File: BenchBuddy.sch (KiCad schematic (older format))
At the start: 0 parts

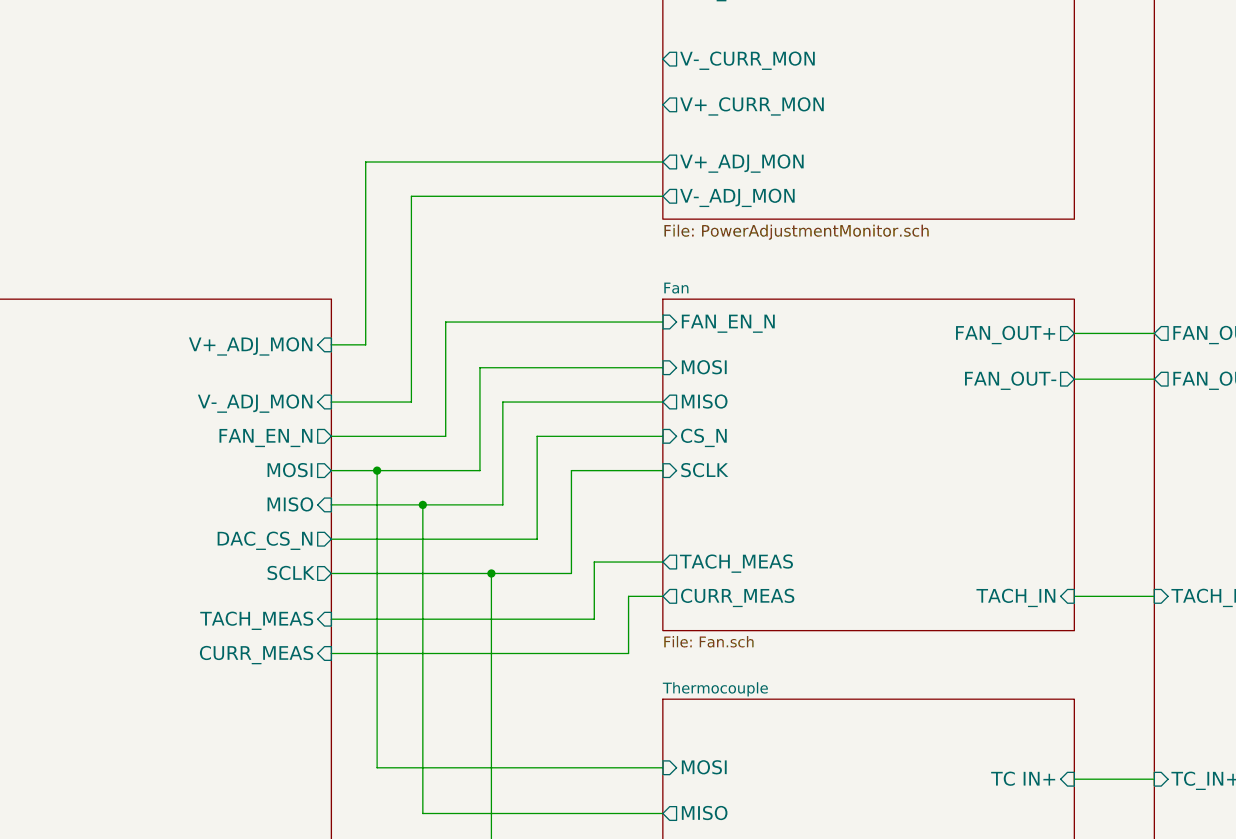
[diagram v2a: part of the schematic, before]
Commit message: Fan/Current Module Refactoring
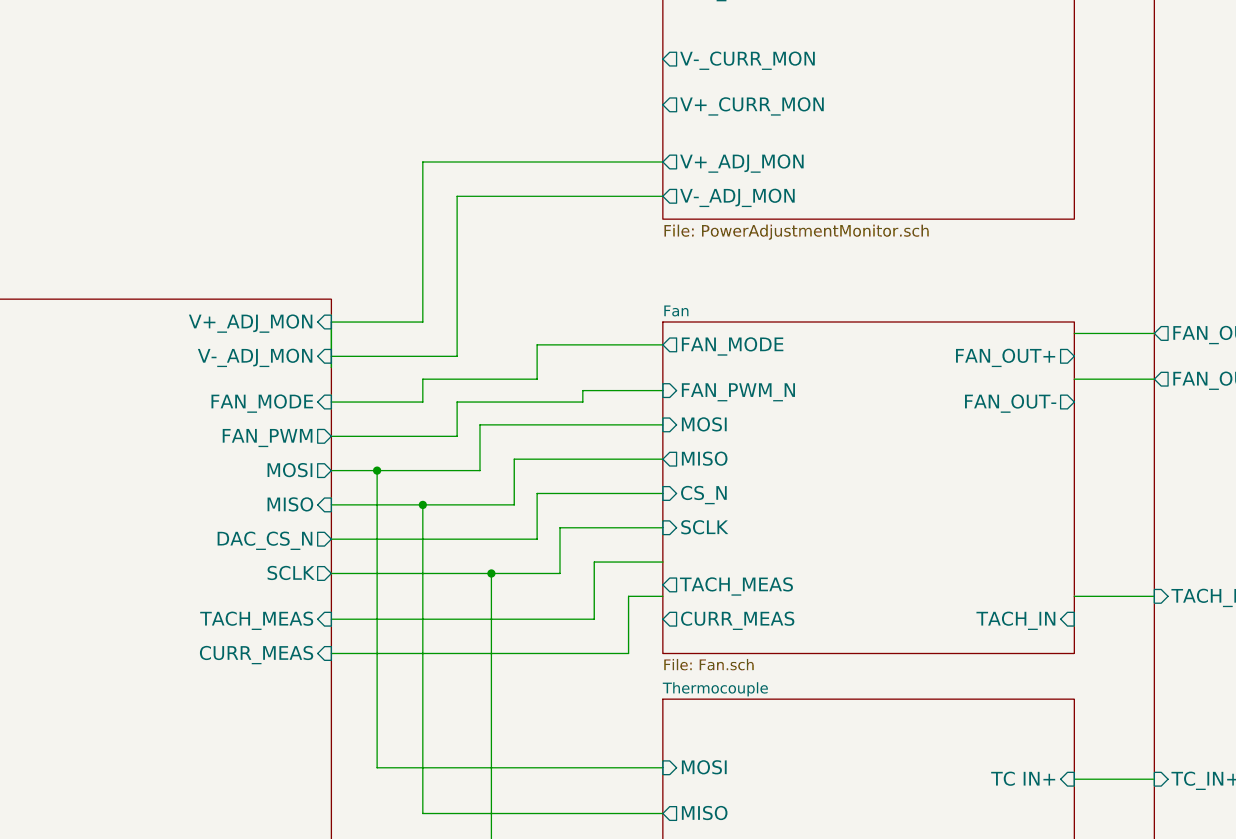
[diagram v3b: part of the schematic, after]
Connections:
- wire segments 55 -> 63
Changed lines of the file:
@@
 Sheet 1 9
 Title ""
-Date "6 feb 2014"
+Date "7 feb 2014"
 Rev ""
 Comp ""
@@
 $EndSheet
 $Sheet
-S 7750 2550 1800 1450
+S 7750 2650 1800 1450
 U 52EBC1E0
 F0 "Fan" 47
 F1 "Fan.sch" 47
-F2 "MOSI" I L 7750 2850 60
-F3 "MISO" O L 7750 3000 60
-F4 "CS_N" I L 7750 3150 60
-F5 "SCLK" I L 7750 3300 60
-F6 "FAN_OUT+" O R 9550 2700 60
-F7 "FAN_OUT-" O R 9550 2900 60
-F8 "TACH_IN" I R 9550 3850 60
-F9 "TACH_MEAS" O L 7750 3700 60
-F10 "FAN_EN_N" I L 7750 2650 60
-F11 "CURR_MEAS" O L 7750 3850 60
+F2 "MOSI" I L 7750 3100 60
+F3 "MISO" O L 7750 3250 60
+F4 "CS_N" I L 7750 3400 60
+F5 "SCLK" I L 7750 3550 60
+F6 "FAN_OUT+" O R 9550 2800 60
+F7 "FAN_OUT-" O R 9550 3000 60
+F8 "TACH_IN" I R 9550 3950 60
+F9 "TACH_MEAS" O L 7750 3800 60
+F10 "CURR_MEAS" O L 7750 3950 60
+F11 "FAN_PWM_N" I L 7750 2950 60
+F12 "FAN_MODE" O L 7750 2750 60
 $EndSheet
 $Sheet
@@
 	9900 3850 9550 3850
 Wire Wire Line
-	6300 2750 6450 2750
-Wire Wire Line
-	6450 2750 6450 1950
-Wire Wire Line
-	6450 1950 7750 1950
-Wire Wire Line
-	6300 3000 6650 3000
-Wire Wire Line
-	6650 3000 6650 2100
-Wire Wire Line
-	6650 2100 7750 2100
-Wire Wire Line
-	6300 3150 6800 3150
-Wire Wire Line
-	6800 3150 6800 2650
-Wire Wire Line
-	6800 2650 7750 2650
+	6300 3150 6850 3150
 Wire Wire Line
 	6300 3300 6950 3300
 Wire Wire Line
-	6950 3300 6950 2850
-Wire Wire Line
-	6950 2850 7750 2850
-Wire Wire Line
-	6300 3450 7050 3450
-Wire Wire Line
-	7050 3450 7050 3000
-Wire Wire Line
-	7050 3000 7750 3000
+	6300 3450 7100 3450
 Wire Wire Line
 	6300 3950 7450 3950
@@
 Wire Wire Line
 	6700 4800 6700 3450
-Connection ~ 6700 3450
 $Sheet
 S 3900 2550 2400 3750
@@
 F6 "SCLK" O R 6300 3750 60
 F7 "TACH_MEAS" I R 6300 3950 60
-F8 "FAN_EN_N" O R 6300 3150 60
-F9 "CURR_MEAS" I R 6300 4100 60
-F10 "V+_ADJ_MON" I R 6300 2750 60
-F11 "V-_ADJ_MON" I R 6300 3000 60
-F12 "LED_EN_PWM" I R 6300 5750 60
-F13 "DAC_CS_N" O R 6300 3600 60
-F14 "ADC_CS_N" I R 6300 5200 60
-$EndSheet
-Wire Wire Line
-	7750 3150 7200 3150
-Wire Wire Line
-	7200 3150 7200 3600
-Wire Wire Line
-	7200 3600 6300 3600
-Wire Wire Line
-	7750 3300 7350 3300
-Wire Wire Line
-	7350 3300 7350 3750
-Wire Wire Line
-	7350 3750 6300 3750
+F8 "CURR_MEAS" I R 6300 4100 60
+F9 "V+_ADJ_MON" I R 6300 2650 60
+F10 "V-_ADJ_MON" I R 6300 2800 60
+F11 "LED_EN_PWM" I R 6300 5750 60
+F12 "DAC_CS_N" O R 6300 3600 60
+F13 "ADC_CS_N" I R 6300 5200 60
+F14 "FAN_PWM" O R 6300 3150 60
+F15 "FAN_MODE" I R 6300 3000 60
+$EndSheet
+Wire Wire Line
+	6300 3750 7300 3750
 Wire Wire Line
 	7750 5000 7000 5000
 Wire Wire Line
 	7000 5000 7000 3750
+Wire Wire Line
+	7750 5200 6300 5200
+Wire Wire Line
+	7750 5750 6300 5750
+Wire Wire Line
+	6300 6050 6950 6050
+Wire Wire Line
+	6950 6050 6950 6600
+Wire Wire Line
+	6950 6600 7750 6600
+Wire Wire Line
+	7750 6850 7750 6700
+Wire Wire Line
+	7750 6700 6650 6700
+Wire Wire Line
+	6650 6700 6650 6200
+Wire Wire Line
+	6650 6200 6300 6200
+Wire Wire Line
+	7750 1950 6700 1950
+Wire Wire Line
+	6700 1950 6700 2650
+Wire Wire Line
+	6700 2650 6300 2650
+Wire Wire Line
+	6300 2650 6300 2850
+Wire Wire Line
+	6300 2800 6850 2800
+Wire Wire Line
+	6850 2800 6850 2100
+Wire Wire Line
+	6850 2100 7750 2100
+Wire Wire Line
+	7750 3550 7300 3550
+Wire Wire Line
+	7300 3550 7300 3750
 Connection ~ 7000 3750
 Wire Wire Line
-	7750 5200 6300 5200
-Wire Wire Line
-	7750 5750 6300 5750
-Wire Wire Line
-	6300 6050 6950 6050
-Wire Wire Line
-	6950 6050 6950 6600
-Wire Wire Line
-	6950 6600 7750 6600
-Wire Wire Line
-	7750 6850 7750 6700
-Wire Wire Line
-	7750 6700 6650 6700
-Wire Wire Line
-	6650 6700 6650 6200
-Wire Wire Line
-	6650 6200 6300 6200
+	6300 3600 7200 3600
+Wire Wire Line
+	7200 3600 7200 3400
+Wire Wire Line
+	7200 3400 7750 3400
+Wire Wire Line
+	7100 3450 7100 3250
+Wire Wire Line
+	7100 3250 7750 3250
+Connection ~ 6700 3450
+Wire Wire Line
+	6950 3300 6950 3100
+Wire Wire Line
+	6950 3100 7750 3100
+Wire Wire Line
+	6850 3150 6850 3000
+Wire Wire Line
+	6850 3000 7400 3000
+Wire Wire Line
+	7400 3000 7400 2950
+Wire Wire Line
+	7400 2950 7750 2950
+Wire Wire Line
+	6300 3000 6700 3000
+Wire Wire Line
+	6700 3000 6700 2900
+Wire Wire Line
+	6700 2900 7200 2900
+Wire Wire Line
+	7200 2900 7200 2750
+Wire Wire Line
+	7200 2750 7750 2750
 $EndSCHEMATC

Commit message: Am Ende der 5. Woche.
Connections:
- wire segments 63 -> 50
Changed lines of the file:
@@
 Sheet 1 9
 Title ""
-Date "17 feb 2014"
+Date "22 feb 2014"
 Rev ""
 Comp ""
@@
 $EndDescr
 $Sheet
-S 7750 4300 1800 1050
+S 7750 4350 1800 1050
 U 52EBC0AD
 F0 "Thermocouple" 47
 F1 "Thermocouple.sch" 47
-F2 "TC IN+" I R 9550 4650 60
-F3 "TC IN-" I R 9550 5000 60
-F4 "MOSI" I L 7750 4600 60
-F5 "MISO" O L 7750 4800 60
-F6 "SCLK" I L 7750 5000 60
-F7 "CS_N" I L 7750 5200 60
+F2 "TC IN+" I R 9550 4700 60
+F3 "TC IN-" I R 9550 5050 60
+F4 "MOSI" I L 7750 4450 60
+F5 "MISO" O L 7750 4600 60
+F6 "SCLK" I L 7750 4750 60
+F7 "~CS" I L 7750 4950 60
+F8 "~RESET" I L 7750 5100 60
+F9 "~DR" O L 7750 5250 60
 $EndSheet
 $Sheet
@@
 $EndSheet
 $Sheet
-S 7750 5650 1800 450
+S 7750 5800 1800 450
 U 52EBC11D
 F0 "LED_Driver" 50
 F1 "LED_Driver.sch" 50
-F2 "LED_EN_PWM" I L 7750 5750 60
-F3 "LED_STRING+" O R 9550 5800 60
-F4 "LED_STRING-" O R 9550 5950 60
+F2 "LED_EN_PWM" I L 7750 5900 60
+F3 "LED_STRING+" O R 9550 5950 60
+F4 "LED_STRING-" O R 9550 6100 60
 $EndSheet
 $Sheet
@@
 F5 "FAN_OUT-" O L 9900 2900 60
 F6 "TACH_IN" I L 9900 3850 60
-F7 "LED_STRING+" O L 9900 5800 60
-F8 "LED_STRING-" O L 9900 5950 60
-F9 "TC_IN+" I L 9900 4650 60
-F10 "TC_IN-" I L 9900 5000 60
+F7 "LED_STRING+" O L 9900 5950 60
+F8 "LED_STRING-" O L 9900 6100 60
+F9 "TC_IN+" I L 9900 4700 60
+F10 "TC_IN-" I L 9900 5050 60
 F11 "RELAY_COM" B L 9900 6550 60
 F12 "RELAY_NC" B L 9900 6700 60
@@
 F0 "Fan" 47
 F1 "Fan.sch" 47
-F2 "MOSI" I L 7750 3100 60
-F3 "MISO" O L 7750 3250 60
-F4 "CS_N" I L 7750 3400 60
-F5 "SCLK" I L 7750 3550 60
-F6 "FAN_OUT+" O R 9550 2800 60
-F7 "FAN_OUT-" O R 9550 3000 60
-F8 "TACH_IN" I R 9550 3950 60
-F9 "TACH_MEAS" O L 7750 3800 60
-F10 "CURR_MEAS" O L 7750 3950 60
-F11 "FAN_PWM_N" I L 7750 2950 60
-F12 "FAN_MODE" O L 7750 2750 60
+F2 "MOSI" I L 7750 3050 60
+F3 "CS_N" I L 7750 3200 60
+F4 "SCLK" I L 7750 3350 60
+F5 "FAN_OUT+" O R 9550 2700 60
+F6 "FAN_OUT-" O R 9550 2900 60
+F7 "TACH_IN" I R 9550 3850 60
+F8 "TACH_MEAS" O L 7750 3850 60
+F9 "CURR_MEAS" O L 7750 4000 60
+F10 "FAN_PWM_N" I L 7750 2900 60
+F11 "FAN_MODE" O L 7750 2750 60
+F12 "~LDAC" I L 7750 3500 60
+F13 "~SHDN" I L 7750 3650 60
 $EndSheet
 $Sheet
@@
 	9900 3850 9550 3850
 Wire Wire Line
-	6300 3150 6850 3150
-Wire Wire Line
-	6300 3300 6950 3300
-Wire Wire Line
-	6300 3450 7100 3450
-Wire Wire Line
-	6300 3950 7450 3950
-Wire Wire Line
-	7450 3950 7450 3700
-Wire Wire Line
-	7450 3700 7750 3700
-Wire Wire Line
-	7750 3850 7600 3850
-Wire Wire Line
-	7600 3850 7600 4100
-Wire Wire Line
-	7600 4100 6300 4100
-Wire Wire Line
-	9550 5500 9550 5450
-Wire Wire Line
-	9550 4650 9900 4650
-Wire Wire Line
-	9900 5000 9550 5000
-Wire Wire Line
-	9900 5800 9550 5800
+	9550 4700 9900 4700
+Wire Wire Line
+	9900 5050 9550 5050
 Wire Wire Line
 	9550 5950 9900 5950
@@
 	9900 6850 9550 6850
 Wire Wire Line
-	7750 4600 6500 4600
-Wire Wire Line
-	6500 4600 6500 3300
-Connection ~ 6500 3300
-Wire Wire Line
-	7750 4800 6700 4800
-Wire Wire Line
-	6700 4800 6700 3450
-$Sheet
-S 3900 2550 2400 3750
+	7750 5900 6300 5900
+Wire Wire Line
+	7750 1950 6700 1950
+Wire Wire Line
+	6700 1950 6700 2650
+Wire Wire Line
+	6700 2650 6300 2650
+Wire Wire Line
+	6300 2800 6850 2800
+Wire Wire Line
+	6850 2800 6850 2100
+Wire Wire Line
+	6850 2100 7750 2100
+$Sheet
+S 3850 2550 2450 4450
 U 52EBBFA9
 F0 "Arduino" 47
 F1 "Arduino.sch" 47
-F2 "Relay+" O R 6300 6050 60
-F3 "Relay-" I R 6300 6200 60
+F2 "Relay+" O R 6300 6600 60
+F3 "Relay-" I R 6300 6800 60
 F4 "MOSI" O R 6300 3300 60
-F5 "MISO" I R 6300 3450 60
-F6 "SCLK" O R 6300 3750 60
-F7 "TACH_MEAS" I R 6300 3950 60
-F8 "CURR_MEAS" I R 6300 4100 60
+F5 "MISO" I R 6300 4600 60
+F6 "SCLK" O R 6300 4750 60
+F7 "TACH_MEAS" I R 6300 3850 60
+F8 "CURR_MEAS" I R 6300 4000 60
 F9 "V+_ADJ_MON" I R 6300 2650 60
 F10 "V-_ADJ_MON" I R 6300 2800 60
-F11 "LED_EN_PWM" I R 6300 5750 60
-F12 "DAC_CS_N" O R 6300 3600 60
-F13 "ADC_CS_N" I R 6300 5200 60
-F14 "FAN_PWM" O R 6300 3150 60
-F15 "FAN_MODE" I R 6300 3000 60
-$EndSheet
-Wire Wire Line
-	6300 3750 7300 3750
-Wire Wire Line
-	7750 5000 7000 5000
-Wire Wire Line
-	7000 5000 7000 3750
-Wire Wire Line
-	7750 5200 6300 5200
-Wire Wire Line
-	7750 5750 6300 5750
-Wire Wire Line
-	6300 6050 6950 6050
-Wire Wire Line
-	6950 6050 6950 6600
-Wire Wire Line
-	6950 6600 7750 6600
-Wire Wire Line
-	7750 6850 7750 6700
-Wire Wire Line
-	7750 6700 6650 6700
-Wire Wire Line
-	6650 6700 6650 6200
-Wire Wire Line
-	6650 6200 6300 6200
-Wire Wire Line
-	7750 1950 6700 1950
-Wire Wire Line
-	6700 1950 6700 2650
-Wire Wire Line
-	6700 2650 6300 2650
-Wire Wire Line
-	6300 2650 6300 2850
-Wire Wire Line
-	6300 2800 6850 2800
-Wire Wire Line
-	6850 2800 6850 2100
-Wire Wire Line
-	6850 2100 7750 2100
-Wire Wire Line
-	7750 3550 7300 3550
-Wire Wire Line
-	7300 3550 7300 3750
-Connection ~ 7000 3750
-Wire Wire Line
-	6300 3600 7200 3600
-Wire Wire Line
-	7200 3600 7200 3400
-Wire Wire Line
-	7200 3400 7750 3400
-Wire Wire Line
-	7100 3450 7100 3250
-Wire Wire Line
-	7100 3250 7750 3250
-Connection ~ 6700 3450
-Wire Wire Line
-	6950 3300 6950 3100
-Wire Wire Line
-	6950 3100 7750 3100
-Wire Wire Line
-	6850 3150 6850 3000
-Wire Wire Line
-	6850 3000 7400 3000
-Wire Wire Line
-	7400 3000 7400 2950
-Wire Wire Line
-	7400 2950 7750 2950
-Wire Wire Line
-	6300 3000 6700 3000
-Wire Wire Line
-	6700 3000 6700 2900
-Wire Wire Line
-	6700 2900 7200 2900
-Wire Wire Line
-	7200 2900 7200 2750
-Wire Wire Line
-	7200 2750 7750 2750
+F11 "LED_EN_PWM" O R 6300 5900 60
+F12 "FAN_PWM" O R 6300 3150 60
+F13 "FAN_MODE" I R 6300 3000 60
+F14 "~RESET" O R 6300 5100 60
+F15 "~DR" O R 6300 5250 60
+F16 "~LDAC" I R 6300 3600 60
+F17 "~SHDN" O R 6300 3750 60
+F18 "~DAC_CS" O R 6300 3450 60
+F19 "~ADC_CS" I R 6300 4950 60
+$EndSheet
+Wire Wire Line
+	9900 6100 9550 6100
+Wire Wire Line
+	6950 3000 6950 2750
+Wire Wire Line
+	6950 2750 7750 2750
+Wire Wire Line
+	7050 2900 7050 3150
+Wire Wire Line
+	7150 3300 7150 3050
+Wire Wire Line
+	7250 3200 7250 3450
+Wire Wire Line
+	7750 3050 7150 3050
+Wire Wire Line
+	7250 3200 7750 3200
+Wire Wire Line
+	7350 3600 7350 3500
+Wire Wire Line
+	7350 3500 7750 3500
+Wire Wire Line
+	7450 3750 7450 3650
+Wire Wire Line
+	7450 3650 7750 3650
+Wire Wire Line
+	6300 5250 7750 5250
+Wire Wire Line
+	7750 5100 6300 5100
+Wire Wire Line
+	6300 4950 7750 4950
+Wire Wire Line
+	6300 4750 7750 4750
+Wire Wire Line
+	7750 4600 6300 4600
+Wire Wire Line
+	7750 4450 6600 4450
+Wire Wire Line
+	6600 4450 6600 3300
+Connection ~ 6600 3300
+Wire Wire Line
+	7750 6800 6300 6800
+Wire Wire Line
+	6300 6600 7750 6600
+Wire Wire Line
+	7750 4000 6300 4000
+Wire Wire Line
+	6300 3850 7750 3850
+Wire Wire Line
+	7450 3750 6300 3750
+Wire Wire Line
+	6300 3600 7350 3600
+Wire Wire Line
+	7250 3450 6300 3450
+Wire Wire Line
+	6300 3300 7150 3300
+Wire Wire Line
+	7050 3150 6300 3150
+Wire Wire Line
+	6950 3000 6300 3000
+Wire Wire Line
+	7750 3350 6950 3350
+Wire Wire Line
+	6950 3350 6950 4750
+Connection ~ 6950 4750
+Wire Wire Line
+	7050 2900 7750 2900
 $EndSCHEMATC
